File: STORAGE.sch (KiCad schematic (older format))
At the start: 10 parts, among them J1101 MICRO_SD_HINGE, U1101 EMIF06-mSD02C3, U1102 MTFC8GACAEAM-1M_WT, U803 MCIMX7D7DVM10SC

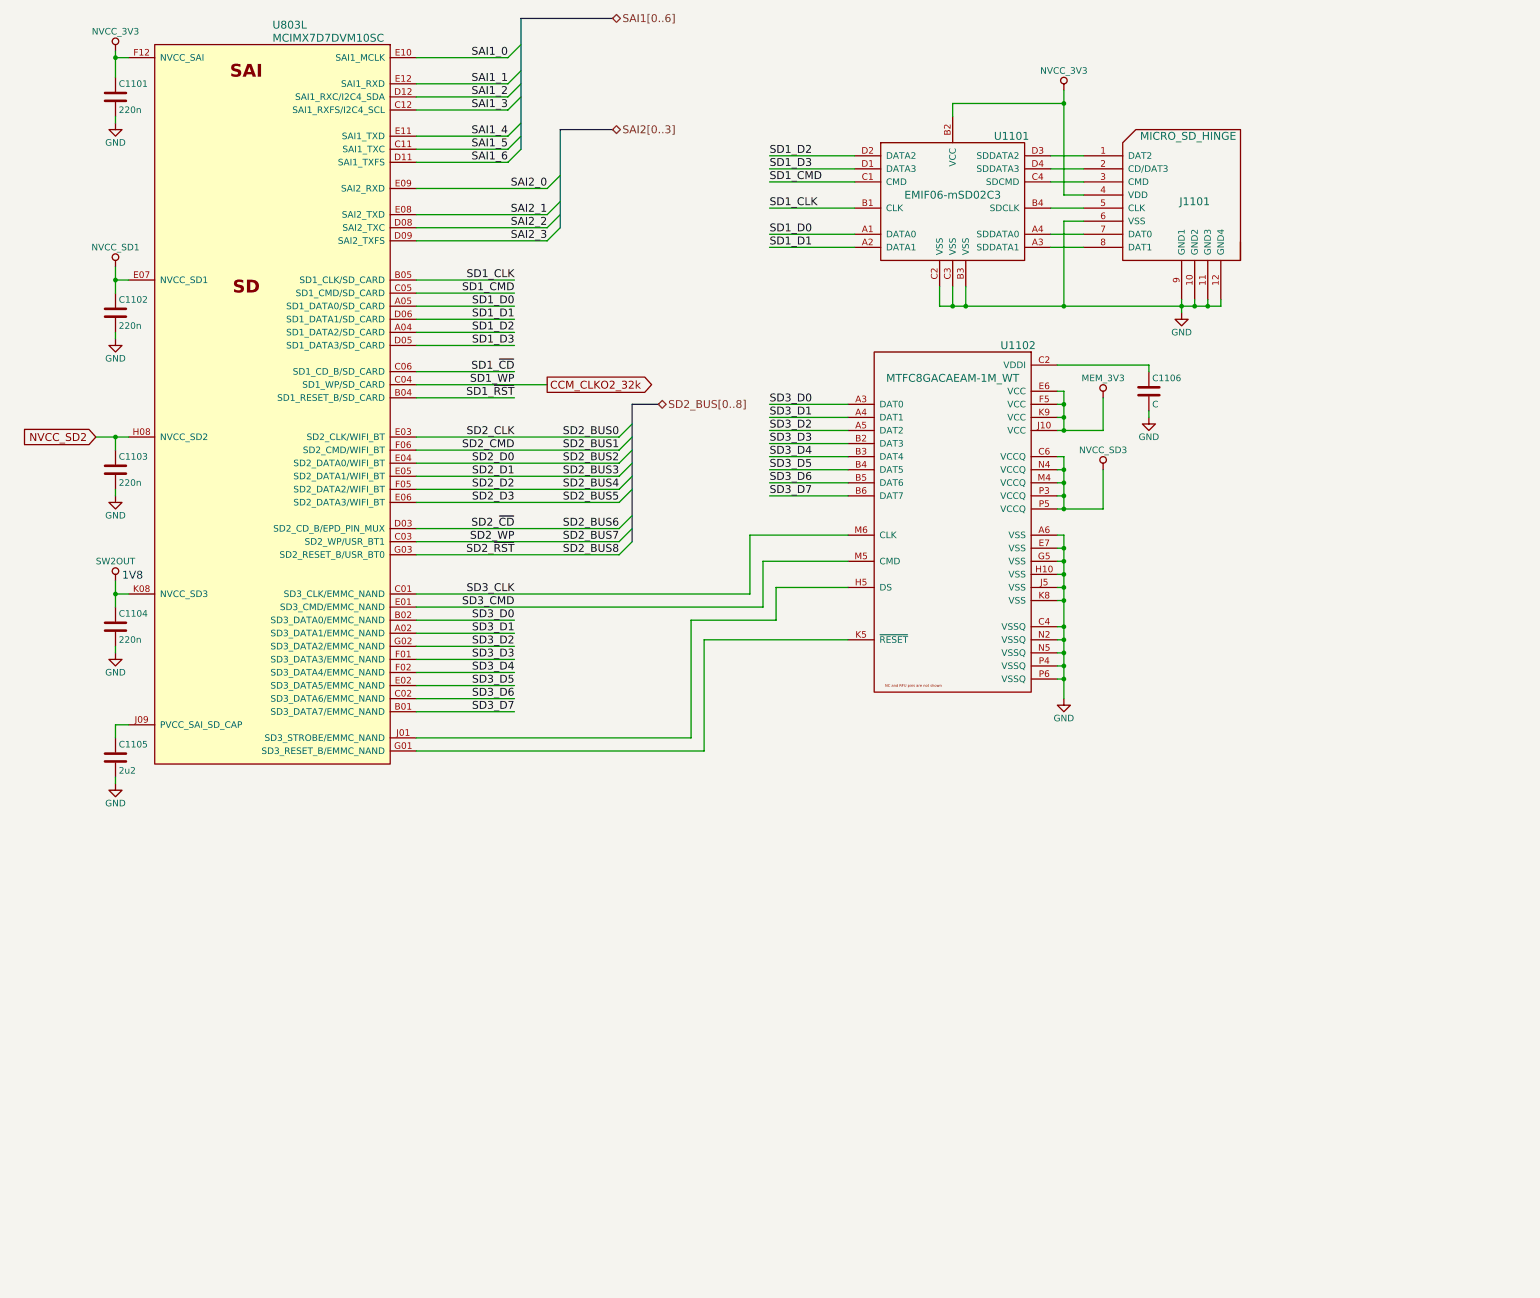
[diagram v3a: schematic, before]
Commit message: Modified power nets Added table of contents
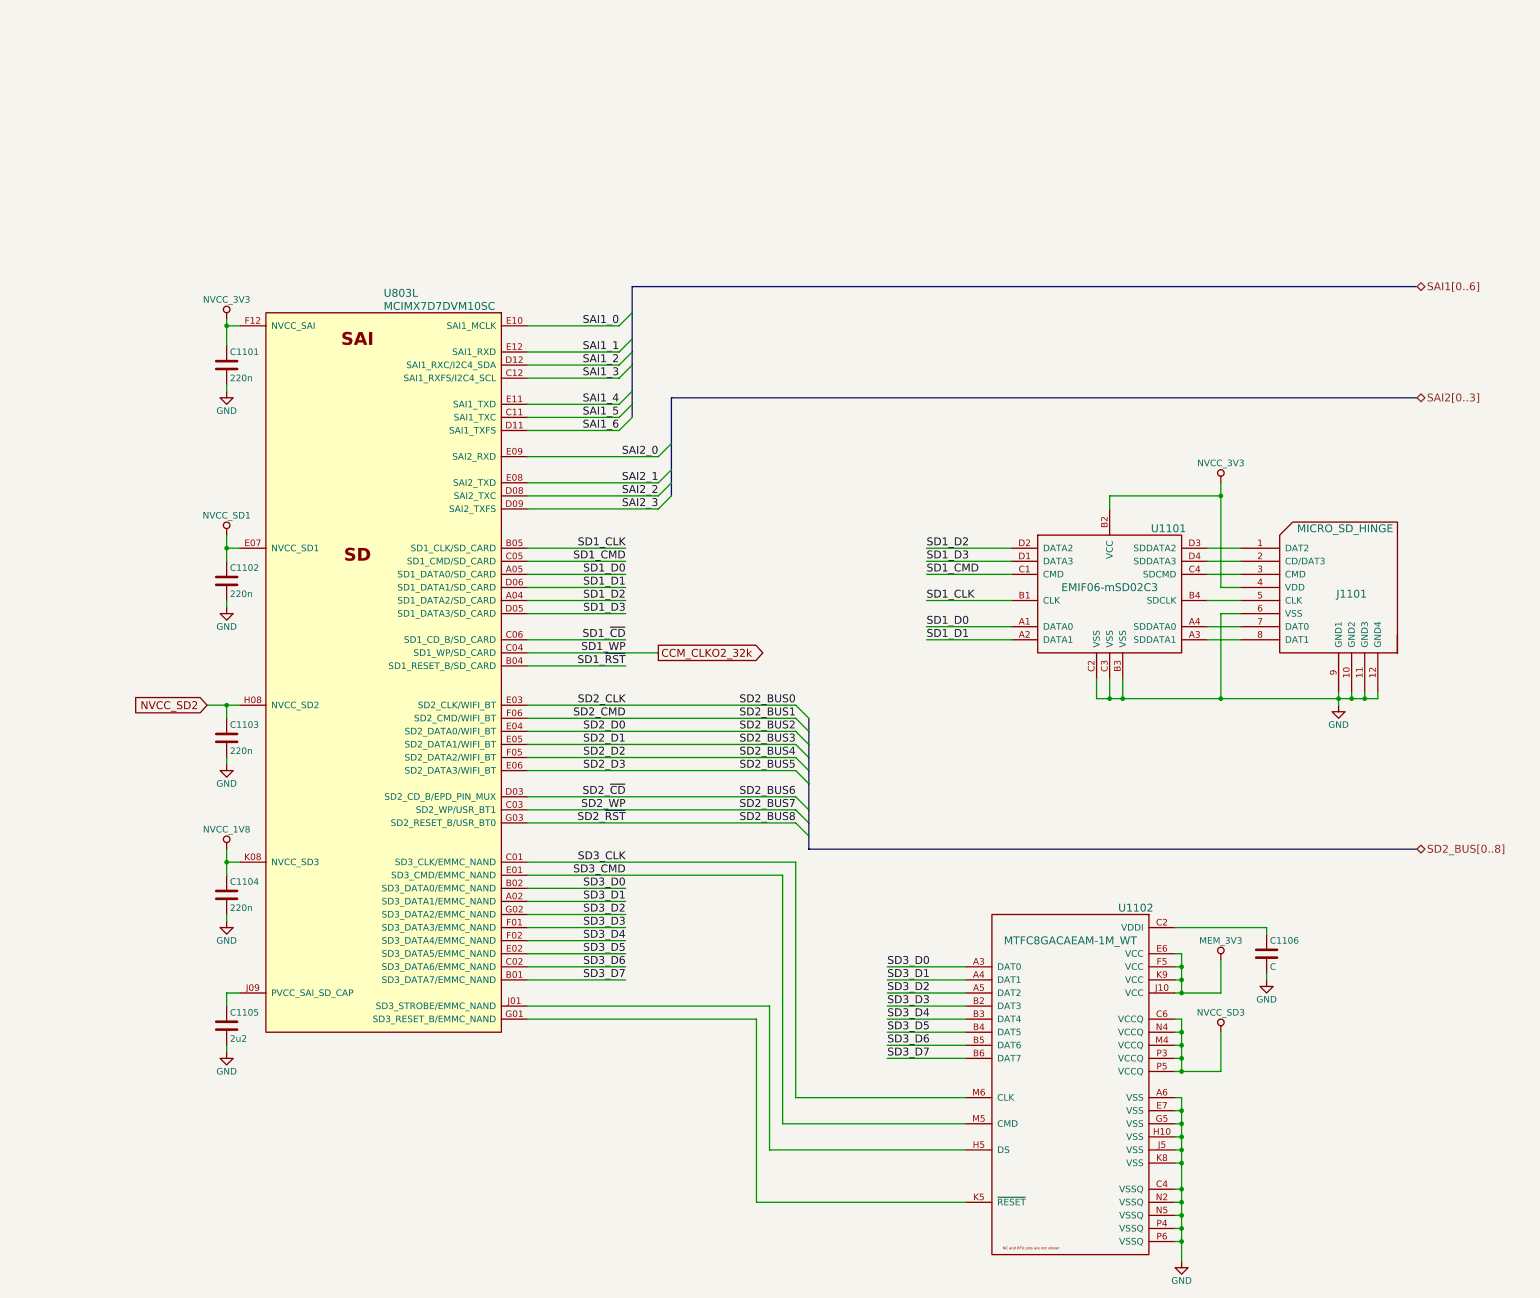
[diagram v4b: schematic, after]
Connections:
- net SW2OUT renamed NVCC_1V8
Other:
- note removed: "1V8"
- moved on the sheet: C1101, C1102, C1103, C1104, C1105, C1106, J1101, U1101, U1102, U803L

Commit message: Changed several voltage rail connections Removed non existing rails Added circuit for NiMH charging
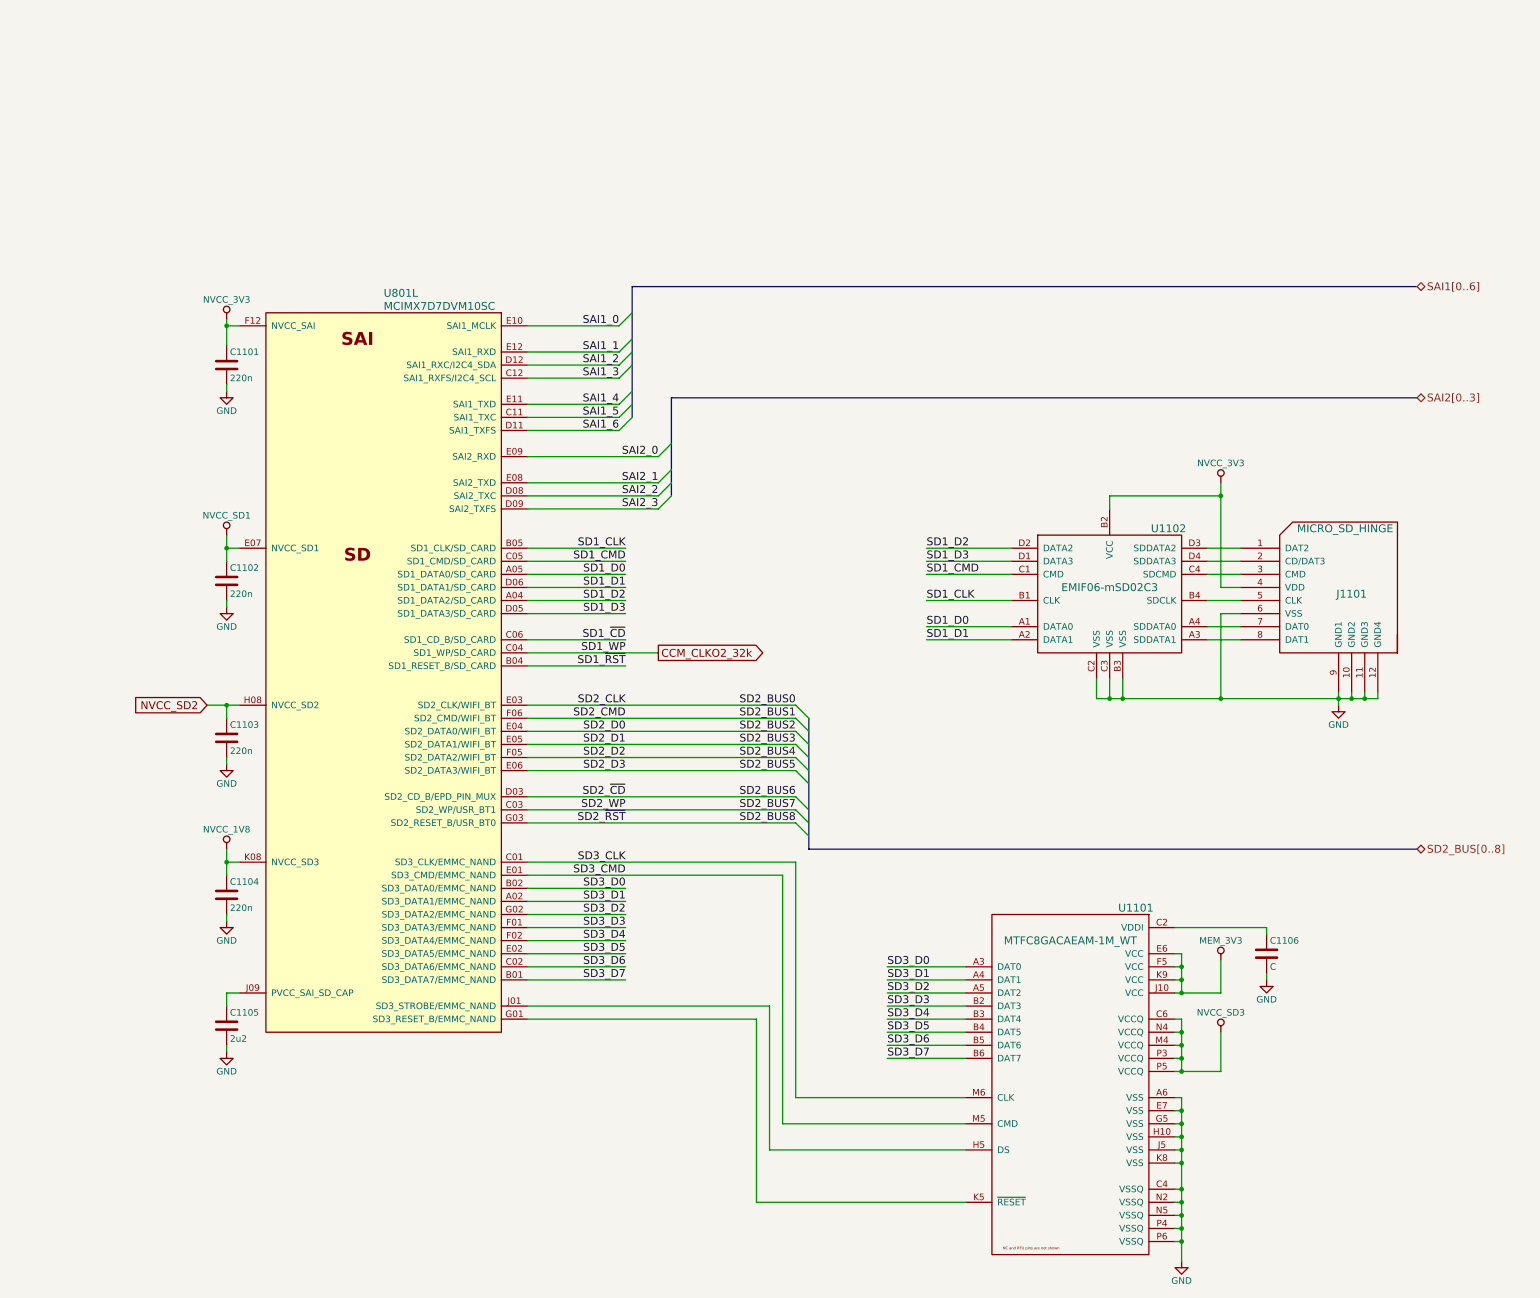
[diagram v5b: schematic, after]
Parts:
- renumbered U1102 to U1101, U1101 to U1102, U803 to U801
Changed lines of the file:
@@
 $EndDescr
 $Comp
-L MCIMX7D7DVM10SC U803
+L MCIMX7D7DVM10SC U801
 U 12 1 594351FC
 P 3900 3000
-F 0 "U803" H 3900 3000 60  0000 L CNN
+F 0 "U801" H 3900 3000 60  0000 L CNN
 F 1 "MCIMX7D7DVM10SC" H 3900 2900 60  0000 L CNN
 F 2 "" H 1650 4700 60  0001 C CNN
@@
 SAI2_0
 Wire Bus Line
-	5800 2950 5800 3150
-Wire Bus Line
-	5800 3150 5800 3350
-Wire Bus Line
-	5800 3350 5800 3450
-Wire Bus Line
-	5800 3450 5800 3550
-Wire Bus Line
-	5800 3550 5800 3750
-Wire Bus Line
-	5800 3750 5800 3850
-Wire Bus Line
-	5800 3850 5800 3950
+	5800 2950 5800 3950
 Wire Bus Line
 	5800 2950 11800 2950
 Wire Bus Line
-	6100 3800 6100 4150
-Wire Bus Line
-	6100 4150 6100 4350
-Wire Bus Line
-	6100 4350 6100 4450
-Wire Bus Line
-	6100 4450 6100 4550
+	6100 3800 6100 4550
 Wire Bus Line
 	6100 3800 11800 3800
@@
 $EndComp
 $Comp
-L GND #PWR1114
+L GND #PWR0262
 U 1 1 5944B647
 P 11200 6150
-F 0 "#PWR1114" H 11200 5900 50  0001 C CNN
+F 0 "#PWR0262" H 11200 5900 50  0001 C CNN
 F 1 "GND" H 11200 6000 50  0000 C CNN
 F 2 "" H 11200 6150 50  0000 C CNN
@@
 $EndComp
 Wire Wire Line
-	11200 6050 11200 6100
-Wire Wire Line
-	11200 6100 11200 6150
-Wire Wire Line
-	9350 6100 9450 6100
-Wire Wire Line
-	9450 6100 9550 6100
-Wire Wire Line
-	9550 6100 10300 6100
-Wire Wire Line
-	10300 6100 11200 6100
-Wire Wire Line
-	11200 6100 11300 6100
-Wire Wire Line
-	11300 6100 11400 6100
-Wire Wire Line
-	11400 6100 11500 6100
+	11200 6050 11200 6150
+Wire Wire Line
+	9350 6100 11500 6100
 Wire Wire Line
 	11500 6100 11500 6050
@@
 	10200 4950 10450 4950
 $Comp
-L EMIF06-mSD02C3 U1101
+L EMIF06-mSD02C3 U1102
 U 1 1 5944C05B
 P 9450 5250
-F 0 "U1101" H 9900 5700 60  0000 C CNN
+F 0 "U1102" H 9900 5700 60  0000 C CNN
 F 1 "EMIF06-mSD02C3" H 9450 5250 60  0000 C CNN
 F 2 "" H 9900 5700 60  0001 C CNN
@@
 $EndComp
 $Comp
-L NVCC_3V3 #PWR1109
+L NVCC_3V3 #PWR0263
 U 1 1 5944C8E9
 P 10300 4450
-F 0 "#PWR1109" H 10300 4300 50  0001 C CNN
+F 0 "#PWR0263" H 10300 4300 50  0001 C CNN
 F 1 "NVCC_3V3" H 10300 4600 50  0000 C CNN
 F 2 "" H 10300 4450 50  0001 C CNN
@@
 	10300 5250 10450 5250
 Wire Wire Line
-	10300 4450 10300 4550
-Wire Wire Line
-	10300 4550 10300 5250
+	10300 4450 10300 5250
 Wire Wire Line
 	10300 4550 9450 4550
@@
 	10650 7850 9950 7850
 $Comp
-L GND #PWR1113
+L GND #PWR0264
 U 1 1 5944DCC6
 P 10650 8250
-F 0 "#PWR1113" H 10650 8000 50  0001 C CNN
+F 0 "#PWR0264" H 10650 8000 50  0001 C CNN
 F 1 "GND" H 10650 8100 50  0000 C CNN
 F 2 "" H 10650 8250 50  0000 C CNN
@@
 	10650 8250 10650 8200
 $Comp
-L MEM_3V3 #PWR1111
+L MEM_3V3 #PWR0265
 U 1 1 5944DD41
 P 10300 8100
-F 0 "#PWR1111" H 10300 7950 50  0001 C CNN
+F 0 "#PWR0265" H 10300 7950 50  0001 C CNN
 F 1 "MEM_3V3" H 10300 8250 50  0000 C CNN
 F 2 "" H 10300 8100 50  0001 C CNN
@@
 	10300 8350 10300 8100
 Wire Wire Line
-	9950 8350 10000 8350
-Wire Wire Line
-	10000 8350 10300 8350
-Wire Wire Line
-	10000 8050 10000 8150
-Wire Wire Line
-	10000 8150 10000 8250
-Wire Wire Line
-	10000 8250 10000 8350
+	9950 8350 10300 8350
+Wire Wire Line
+	10000 8050 10000 8350
 Wire Wire Line
 	10000 8050 9950 8050
@@
 Connection ~ 10000 8250
 $Comp
-L MTFC8GACAEAM-1M_WT U1102
+L MTFC8GACAEAM-1M_WT U1101
 U 1 1 5944D61A
 P 9150 7950
-F 0 "U1102" H 9650 8200 60  0000 C CNN
+F 0 "U1101" H 9650 8200 60  0000 C CNN
 F 1 "MTFC8GACAEAM-1M_WT" H 9150 7950 60  0000 C CNN
 F 2 "" H 9950 8200 60  0001 C CNN
@@
 	9950 8550 10000 8550
 Wire Wire Line
-	10000 8550 10000 8650
-Wire Wire Line
-	10000 8650 10000 8750
-Wire Wire Line
-	10000 8750 10000 8850
-Wire Wire Line
-	10000 8850 10000 8950
-Wire Wire Line
-	9950 8950 10000 8950
-Wire Wire Line
-	10000 8950 10300 8950
+	10000 8550 10000 8950
+Wire Wire Line
+	9950 8950 10300 8950
 Wire Wire Line
 	9950 8850 10000 8850
@@
 Connection ~ 10000 8950
 $Comp
-L NVCC_SD3 #PWR1112
+L NVCC_SD3 #PWR0266
 U 1 1 5944E338
 P 10300 8650
-F 0 "#PWR1112" H 10300 8500 50  0001 C CNN
+F 0 "#PWR0266" H 10300 8500 50  0001 C CNN
 F 1 "NVCC_SD3" H 10300 8800 50  0000 C CNN
 F 2 "" H 10300 8650 50  0001 C CNN
@@
 	9950 9150 10000 9150
 Wire Wire Line
-	10000 9150 10000 9250
-Wire Wire Line
-	10000 9250 10000 9350
-Wire Wire Line
-	10000 9350 10000 9450
-Wire Wire Line
-	10000 9450 10000 9550
-Wire Wire Line
-	10000 9550 10000 9650
-Wire Wire Line
-	10000 9650 10000 9850
-Wire Wire Line
-	10000 9850 10000 9950
-Wire Wire Line
-	10000 9950 10000 10050
-Wire Wire Line
-	10000 10050 10000 10150
-Wire Wire Line
-	10000 10150 10000 10250
-Wire Wire Line
-	10000 10250 10000 10400
+	10000 9150 10000 10400
 Wire Wire Line
 	9950 9250 10000 9250
@@
 	9950 10250 10000 10250
 $Comp
-L GND #PWR1110
+L GND #PWR0267
 U 1 1 5944E514
 P 10000 10400
-F 0 "#PWR1110" H 10000 10150 50  0001 C CNN
+F 0 "#PWR0267" H 10000 10150 50  0001 C CNN
 F 1 "GND" H 10000 10250 50  0000 C CNN
 F 2 "" H 10000 10400 50  0000 C CNN
@@
 	2800 3250 2700 3250
 Wire Wire Line
-	2700 3200 2700 3250
-Wire Wire Line
-	2700 3250 2700 3400
-$Comp
-L NVCC_3V3 #PWR1101
+	2700 3200 2700 3400
+$Comp
+L NVCC_3V3 #PWR0268
 U 1 1 5944EF86
 P 2700 3200
-F 0 "#PWR1101" H 2700 3050 50  0001 C CNN
+F 0 "#PWR0268" H 2700 3050 50  0001 C CNN
 F 1 "NVCC_3V3" H 2700 3350 50  0000 C CNN
 F 2 "" H 2700 3200 50  0001 C CNN
@@
 Connection ~ 2700 3250
 $Comp
-L GND #PWR1102
+L GND #PWR0269
 U 1 1 5944F032
 P 2700 3750
-F 0 "#PWR1102" H 2700 3500 50  0001 C CNN
+F 0 "#PWR0269" H 2700 3500 50  0001 C CNN
 F 1 "GND" H 2700 3600 50  0000 C CNN
 F 2 "" H 2700 3750 50  0000 C CNN
@@
 	2700 6150 2700 6250
 $Comp
-L GND #PWR1105
+L GND #PWR0270
 U 1 1 5944F9FC
 P 2700 6600
-F 0 "#PWR1105" H 2700 6350 50  0001 C CNN
+F 0 "#PWR0270" H 2700 6350 50  0001 C CNN
 F 1 "GND" H 2700 6450 50  0000 C CNN
 F 2 "" H 2700 6600 50  0000 C CNN
@@
 $EndComp
 Wire Wire Line
-	2700 4850 2700 4950
-Wire Wire Line
-	2700 4950 2700 5050
-$Comp
-L GND #PWR1104
+	2700 4850 2700 5050
+$Comp
+L GND #PWR0271
 U 1 1 5944FABA
 P 2700 5400
-F 0 "#PWR1104" H 2700 5150 50  0001 C CNN
+F 0 "#PWR0271" H 2700 5150 50  0001 C CNN
 F 1 "GND" H 2700 5250 50  0000 C CNN
 F 2 "" H 2700 5400 50  0000 C CNN
@@
 $EndComp
 Wire Wire Line
-	2700 7250 2700 7350
-Wire Wire Line
-	2700 7350 2700 7450
-$Comp
-L GND #PWR1107
+	2700 7250 2700 7450
+$Comp
+L GND #PWR0272
 U 1 1 5944FB14
 P 2700 7800
-F 0 "#PWR1107" H 2700 7550 50  0001 C CNN
+F 0 "#PWR0272" H 2700 7550 50  0001 C CNN
 F 1 "GND" H 2700 7650 50  0000 C CNN
 F 2 "" H 2700 7800 50  0000 C CNN
@@
 	2700 8350 2700 8450
 $Comp
-L GND #PWR1108
+L GND #PWR0273
 U 1 1 5944FC97
 P 2700 8800
-F 0 "#PWR1108" H 2700 8550 50  0001 C CNN
+F 0 "#PWR0273" H 2700 8550 50  0001 C CNN
 F 1 "GND" H 2700 8650 50  0000 C CNN
 F 2 "" H 2700 8800 50  0000 C CNN
@@
 Connection ~ 2700 7350
 Wire Wire Line
-	2550 6150 2700 6150
-Wire Wire Line
-	2700 6150 2800 6150
+	2550 6150 2800 6150
 Connection ~ 2700 6150
 Wire Wire Line
@@
 Connection ~ 2700 4950
 $Comp
-L NVCC_SD1 #PWR1103
+L NVCC_SD1 #PWR0274
 U 1 1 594500AD
 P 2700 4850
-F 0 "#PWR1103" H 2700 4700 50  0001 C CNN
+F 0 "#PWR0274" H 2700 4700 50  0001 C CNN
 F 1 "NVCC_SD1" H 2700 5000 50  0000 C CNN
 F 2 "" H 2700 4850 50  0001 C CNN
@@
 	7050 6950 7150 7050
 Wire Bus Line
-	7150 6250 7150 6350
-Wire Bus Line
-	7150 6350 7150 6450
-Wire Bus Line
-	7150 6450 7150 6550
-Wire Bus Line
-	7150 6550 7150 6650
-Wire Bus Line
-	7150 6650 7150 6750
-Wire Bus Line
-	7150 6750 7150 6950
-Wire Bus Line
-	7150 6950 7150 7050
-Wire Bus Line
-	7150 7050 7150 7150
-Wire Bus Line
-	7150 7150 7150 7250
+	7150 6250 7150 7250
 Text GLabel 2550 6150 0    60   Input ~ 0
 NVCC_SD2
@@
 	7050 9150 8350 9150
 $Comp
-L NVCC_1V8 #PWR?
+L NVCC_1V8 #PWR0275
 U 1 1 595BDAEA
 P 2700 7250
-F 0 "#PWR?" H 2700 7100 50  0001 C CNN
+F 0 "#PWR0275" H 2700 7100 50  0001 C CNN
 F 1 "NVCC_1V8" H 2700 7400 50  0000 C CNN
 F 2 "" H 2700 7250 50  0001 C CNN
